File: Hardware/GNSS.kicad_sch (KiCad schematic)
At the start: 20 parts, among them J1 U.FL_SMD, Q3 BSS138, U13 74HC4052D, U2 mosaic-X5

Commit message: Work in progress...
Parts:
- added TP15, TP16, TP17, TP18: 1.0mm, SparkFun-Connector:TestPoint-1.0mm, symbol SparkFun-Connector:TestPoint_1.0mm
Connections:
- net ESP13/MTX1: now also TP15.1
- net ESP14/MRX1: now also TP16.1
- net ESP25/MRX4: now also TP17.1
- net ESP4/MTX4: now also TP18.1
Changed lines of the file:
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@@
   (junction (at 57.15 97.79) (diameter 0) (color 0 0 0 0)
   )
+  (junction (at 92.71 36.83) (diameter 0) (color 0 0 0 0)
+  )
   (junction (at 231.14 128.27) (diameter 0) (color 0 0 0 0)
   )
+  (junction (at 92.71 34.29) (diameter 0) (color 0 0 0 0)
+  )
   (junction (at 210.82 128.27) (diameter 0) (color 0 0 0 0)
   )
@@
   (junction (at 48.26 113.03) (diameter 0) (color 0 0 0 0)
   )
+  (junction (at 93.98 71.12) (diameter 0) (color 0 0 0 0)
+  )
   (junction (at 36.83 34.29) (diameter 0) (color 0 0 0 0)
   )
+  (junction (at 92.71 73.66) (diameter 0) (color 0 0 0 0)
+  )
   (wire (pts (xy 91.44 77.47) (xy 92.71 77.47))
     (stroke (width 0) (type default))
@@
     (stroke (width 0) (type default))
   )
+  (wire (pts (xy 95.25 66.04) (xy 92.71 66.04))
+    (stroke (width 0) (type default))
+  )
   (wire (pts (xy 22.86 86.36) (xy 22.86 85.09))
     (stroke (width 0) (type default))
@@
     (stroke (width 0) (type default))
   )
+  (wire (pts (xy 92.71 66.04) (xy 92.71 73.66))
+    (stroke (width 0) (type default))
+  )
   (wire (pts (xy 57.15 97.79) (xy 58.42 97.79))
     (stroke (width 0) (type default))
   )
+  (wire (pts (xy 92.71 31.75) (xy 92.71 34.29))
+    (stroke (width 0) (type default))
+  )
   (wire (pts (xy 55.88 97.79) (xy 57.15 97.79))
     (stroke (width 0) (type default))
   )
+  (wire (pts (xy 93.98 71.12) (xy 95.25 71.12))
+    (stroke (width 0) (type default))
+  )
   (wire (pts (xy 210.82 128.27) (xy 212.09 128.27))
     (stroke (width 0) (type default))
@@
     (stroke (width 0) (type default))
   )
-  (wire (pts (xy 91.44 71.12) (xy 92.71 71.12))
+  (wire (pts (xy 91.44 71.12) (xy 93.98 71.12))
     (stroke (width 0) (type default))
   )
@@
     (stroke (width 0) (type default))
   )
+  (wire (pts (xy 92.71 34.29) (xy 93.98 34.29))
+    (stroke (width 0) (type default))
+  )
   (wire (pts (xy 29.21 71.12) (xy 29.21 69.85))
     (stroke (width 0) (type default))
@@
     (stroke (width 0) (type default))
   )
+  (wire (pts (xy 92.71 36.83) (xy 92.71 39.37))
+    (stroke (width 0) (type default))
+  )
   (wire (pts (xy 223.52 128.27) (xy 231.14 128.27))
     (stroke (width 0) (type default))
@@
     (stroke (width 0) (type default))
   )
+  (wire (pts (xy 93.98 39.37) (xy 92.71 39.37))
+    (stroke (width 0) (type default))
+  )
   (wire (pts (xy 210.82 38.1) (xy 214.63 38.1))
     (stroke (width 0) (type default))
   )
+  (wire (pts (xy 93.98 68.58) (xy 93.98 71.12))
+    (stroke (width 0) (type default))
+  )
   (wire (pts (xy 34.29 34.29) (xy 36.83 34.29))
     (stroke (width 0) (type default))
@@
     (stroke (width 0) (type default))
   )
+  (wire (pts (xy 92.71 73.66) (xy 95.25 73.66))
+    (stroke (width 0) (type default))
+  )
   (wire (pts (xy 36.83 24.13) (xy 36.83 25.4))
     (stroke (width 0) (type default))
@@
     (stroke (width 0) (type default))
   )
+  (wire (pts (xy 95.25 68.58) (xy 93.98 68.58))
+    (stroke (width 0) (type default))
+  )
   (wire (pts (xy 87.63 167.64) (xy 86.36 167.64))
     (stroke (width 0) (type default))
@@
     (stroke (width 0) (type default))
   )
+  (wire (pts (xy 92.71 36.83) (xy 93.98 36.83))
+    (stroke (width 0) (type default))
+  )
   (wire (pts (xy 91.44 80.01) (xy 92.71 80.01))
     (stroke (width 0) (type default))
@@
   )
   (wire (pts (xy 57.15 44.45) (xy 57.15 48.26))
+    (stroke (width 0) (type default))
+  )
+  (wire (pts (xy 93.98 31.75) (xy 92.71 31.75))
     (stroke (width 0) (type default))
   )
@@
     )
   )
-  (global_label "ESP14{slash}MRX1" (shape input) (at 92.71 34.29 0) (fields_autoplaced)
-    (effects (font (size 1.27 1.27)) (justify left))
-    (property "Intersheetrefs" "${INTERSHEET_REFS}" (at 107.0041 34.29 0)
+  (global_label "ESP14{slash}MRX1" (shape input) (at 93.98 34.29 0) (fields_autoplaced)
+    (effects (font (size 1.27 1.27)) (justify left))
+    (property "Intersheetrefs" "${INTERSHEET_REFS}" (at 108.2741 34.29 0)
       (effects (font (size 1.27 1.27)) (justify left) hide)
     )
@@
     )
   )
-  (global_label "ESP25{slash}MRX4" (shape input) (at 92.71 71.12 0) (fields_autoplaced)
-    (effects (font (size 1.27 1.27)) (justify left))
-    (property "Intersheetrefs" "${INTERSHEET_REFS}" (at 108.2136 71.12 0)
+  (global_label "ESP25{slash}MRX4" (shape input) (at 95.25 71.12 0) (fields_autoplaced)
+    (effects (font (size 1.27 1.27)) (justify left))
+    (property "Intersheetrefs" "${INTERSHEET_REFS}" (at 110.7536 71.12 0)
       (effects (font (size 1.27 1.27)) (justify left) hide)
     )
@@
     )
   )
-  (global_label "ESP4{slash}MTX4" (shape input) (at 92.71 73.66 0) (fields_autoplaced)
-    (effects (font (size 1.27 1.27)) (justify left))
-    (property "Intersheetrefs" "${INTERSHEET_REFS}" (at 106.7017 73.66 0)
+  (global_label "ESP4{slash}MTX4" (shape input) (at 95.25 73.66 0) (fields_autoplaced)
+    (effects (font (size 1.27 1.27)) (justify left))
+    (property "Intersheetrefs" "${INTERSHEET_REFS}" (at 109.2417 73.66 0)
       (effects (font (size 1.27 1.27)) (justify left) hide)
     )
@@
     )
   )
-  (global_label "ESP13{slash}MTX1" (shape input) (at 92.71 36.83 0) (fields_autoplaced)
-    (effects (font (size 1.27 1.27)) (justify left))
-    (property "Intersheetrefs" "${INTERSHEET_REFS}" (at 106.7017 36.83 0)
+  (global_label "ESP13{slash}MTX1" (shape input) (at 93.98 36.83 0) (fields_autoplaced)
+    (effects (font (size 1.27 1.27)) (justify left))
+    (property "Intersheetrefs" "${INTERSHEET_REFS}" (at 107.9717 36.83 0)
       (effects (font (size 1.27 1.27)) (justify left) hide)
     )
@@
     )
   )
+  (symbol (lib_id "SparkFun-Connector:TestPoint_1.0mm") (at 93.98 31.75 270) (unit 1)
+    (in_bom yes) (on_board yes) (dnp no) (fields_autoplaced)
+    (property "Reference" "TP16" (at 99.06 31.75 90)
+      (effects (font (size 1.27 1.27)) (justify left))
+    )
+    (property "Value" "1.0mm" (at 90.17 31.75 0)
+      (effects (font (size 1.27 1.27)) hide)
+    )
+    (property "Footprint" "SparkFun-Connector:TestPoint-1.0mm" (at 87.63 31.75 0)
+      (effects (font (size 1.27 1.27)) hide)
+    )
+    (property "Datasheet" "~" (at 86.36 31.75 0)
+      (effects (font (size 1.27 1.27)) hide)
+    )
+    (pin "1")
+    (instances
+      (project "SparkFun_RTK_Facet_mosaic"
+        (path "/e3dd3ae4-244d-4cba-9cca-5d2abf83f29a/1004b21d-c362-4c5d-adad-4952c3ff3811"
+          (reference "TP16") (unit 1)
+        )
+      )
+    )
+  )
   (symbol (lib_id "SparkFun-Resistor:10k_0402") (at 53.34 115.57 0) (unit 1)
     (in_bom yes) (on_board yes) (dnp no)
@@
         (path "/e3dd3ae4-244d-4cba-9cca-5d2abf83f29a/1004b21d-c362-4c5d-adad-4952c3ff3811"
           (reference "#PWR010") (unit 1)
+        )
+      )
+    )
+  )
+  (symbol (lib_id "SparkFun-Connector:TestPoint_1.0mm") (at 93.98 39.37 270) (unit 1)
+    (in_bom yes) (on_board yes) (dnp no) (fields_autoplaced)
+    (property "Reference" "TP15" (at 97.282 41.91 90)
+      (effects (font (size 1.27 1.27)))
+    )
+    (property "Value" "1.0mm" (at 90.17 39.37 0)
+      (effects (font (size 1.27 1.27)) hide)
+    )
+    (property "Footprint" "SparkFun-Connector:TestPoint-1.0mm" (at 87.63 39.37 0)
+      (effects (font (size 1.27 1.27)) hide)
+    )
+    (property "Datasheet" "~" (at 86.36 39.37 0)
+      (effects (font (size 1.27 1.27)) hide)
+    )
+    (pin "1")
+    (instances
+      (project "SparkFun_RTK_Facet_mosaic"
+        (path "/e3dd3ae4-244d-4cba-9cca-5d2abf83f29a/1004b21d-c362-4c5d-adad-4952c3ff3811"
+          (reference "TP15") (unit 1)
         )
       )
@@
     )
   )
+  (symbol (lib_id "SparkFun-Connector:TestPoint_1.0mm") (at 95.25 68.58 270) (unit 1)
+    (in_bom yes) (on_board yes) (dnp no) (fields_autoplaced)
+    (property "Reference" "TP17" (at 100.33 68.58 90)
+      (effects (font (size 1.27 1.27)) (justify left))
+    )
+    (property "Value" "1.0mm" (at 91.44 68.58 0)
+      (effects (font (size 1.27 1.27)) hide)
+    )
+    (property "Footprint" "SparkFun-Connector:TestPoint-1.0mm" (at 88.9 68.58 0)
+      (effects (font (size 1.27 1.27)) hide)
+    )
+    (property "Datasheet" "~" (at 87.63 68.58 0)
+      (effects (font (size 1.27 1.27)) hide)
+    )
+    (pin "1")
+    (instances
+      (project "SparkFun_RTK_Facet_mosaic"
+        (path "/e3dd3ae4-244d-4cba-9cca-5d2abf83f29a/1004b21d-c362-4c5d-adad-4952c3ff3811"
+          (reference "TP17") (unit 1)
+        )
+      )
+    )
+  )
   (symbol (lib_id "SparkFun-Capacitor:22uF_0603_6.3V_20%") (at 29.21 66.04 0) (unit 1)
     (in_bom yes) (on_board yes) (dnp no) (fields_autoplaced)
@@
         )
       )
+    )
+  )
+  (symbol (lib_id "SparkFun-Connector:TestPoint_1.0mm") (at 95.25 66.04 270) (unit 1)
+    (in_bom yes) (on_board yes) (dnp no) (fields_autoplaced)
+    (property "Reference" "TP18" (at 100.33 66.04 90)
+      (effects (font (size 1.27 1.27)) (justify left))
+    )
+    (property "Value" "1.0mm" (at 91.44 66.04 0)
+      (effects (font (size 1.27 1.27)) hide)
+    )
+    (property "Footprint" "SparkFun-Connector:TestPoint-1.0mm" (at 88.9 66.04 0)
+      (effects (font (size 1.27 1.27)) hide)
+    )
+    (property "Datasheet" "~" (at 87.63 66.04 0)
+      (effects (font (size 1.27 1.27)) hide)
+    )
+    (pin "1")
+    (instances
+      (project "SparkFun_RTK_Facet_mosaic"
+        (path "/e3dd3ae4-244d-4cba-9cca-5d2abf83f29a/1004b21d-c362-4c5d-adad-4952c3ff3811"
+          (reference "TP18") (unit 1)
+        )
+      )

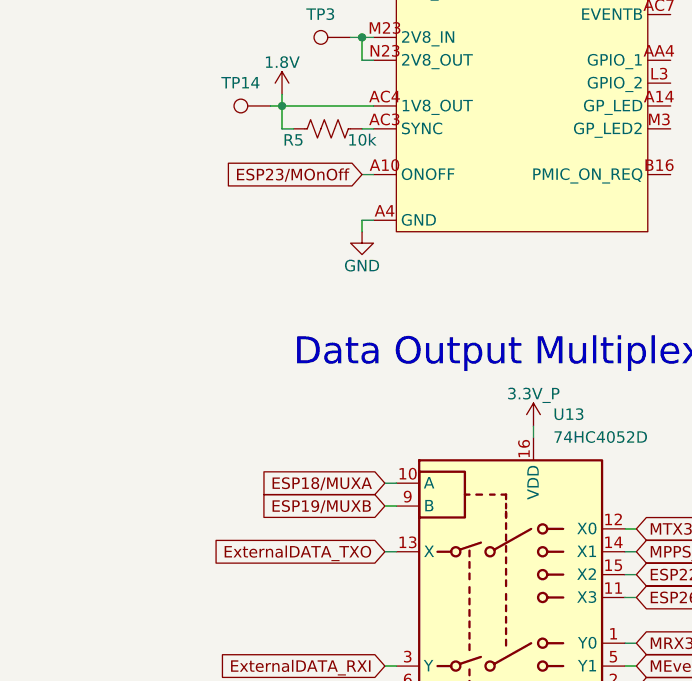
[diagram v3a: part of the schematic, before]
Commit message: Do over with RSP32 Pico Mini - routed
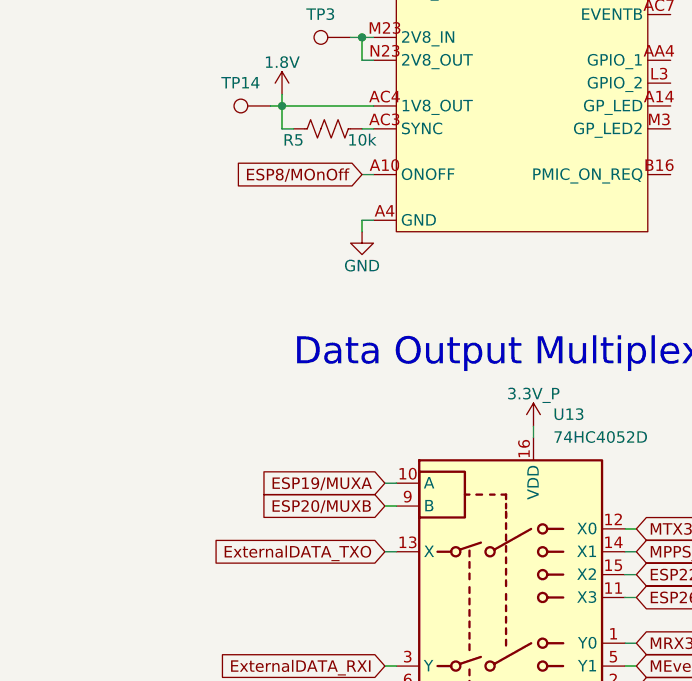
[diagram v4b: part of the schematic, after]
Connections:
- net ESP18/MUXA renamed ESP19/MUXA
- net ESP19/MUXB renamed ESP20/MUXB
- net ESP23/MOnOff renamed ESP8/MOnOff
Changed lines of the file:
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@@
     )
   )
-  (global_label "ESP19{slash}MUXB" (shape input) (at 59.69 157.48 180) (fields_autoplaced)
+  (global_label "ESP20{slash}MUXB" (shape input) (at 59.69 157.48 180) (fields_autoplaced)
     (effects (font (size 1.27 1.27)) (justify right))
     (property "Intersheetrefs" "${INTERSHEET_REFS}" (at 44.0654 157.48 0)
@@
     )
   )
-  (global_label "ESP23{slash}MOnOff" (shape input) (at 57.15 120.65 180) (fields_autoplaced)
+  (global_label "ESP8{slash}MOnOff" (shape input) (at 57.15 120.65 180) (fields_autoplaced)
     (effects (font (size 1.27 1.27)) (justify right))
     (property "Intersheetrefs" "${INTERSHEET_REFS}" (at 40.074 120.65 0)
@@
     )
   )
-  (global_label "ESP18{slash}MUXA" (shape input) (at 59.69 154.94 180) (fields_autoplaced)
+  (global_label "ESP19{slash}MUXA" (shape input) (at 59.69 154.94 180) (fields_autoplaced)
     (effects (font (size 1.27 1.27)) (justify right))
     (property "Intersheetrefs" "${INTERSHEET_REFS}" (at 44.2468 154.94 0)

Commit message: Switching back to the WROVER - routed
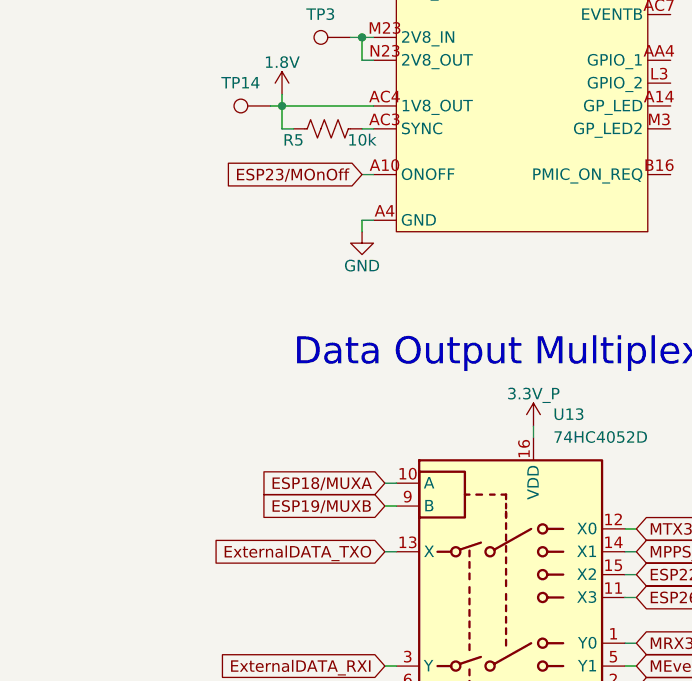
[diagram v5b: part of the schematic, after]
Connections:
- net ESP19/MUXA renamed ESP18/MUXA
- net ESP20/MUXB renamed ESP19/MUXB
- net ESP8/MOnOff renamed ESP23/MOnOff
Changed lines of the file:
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@@
     )
   )
-  (global_label "ESP20{slash}MUXB" (shape input) (at 59.69 157.48 180) (fields_autoplaced)
+  (global_label "ESP19{slash}MUXB" (shape input) (at 59.69 157.48 180) (fields_autoplaced)
     (effects (font (size 1.27 1.27)) (justify right))
     (property "Intersheetrefs" "${INTERSHEET_REFS}" (at 44.0654 157.48 0)
@@
     )
   )
-  (global_label "ESP8{slash}MOnOff" (shape input) (at 57.15 120.65 180) (fields_autoplaced)
+  (global_label "ESP23{slash}MOnOff" (shape input) (at 57.15 120.65 180) (fields_autoplaced)
     (effects (font (size 1.27 1.27)) (justify right))
     (property "Intersheetrefs" "${INTERSHEET_REFS}" (at 40.074 120.65 0)
@@
     )
   )
-  (global_label "ESP19{slash}MUXA" (shape input) (at 59.69 154.94 180) (fields_autoplaced)
+  (global_label "ESP18{slash}MUXA" (shape input) (at 59.69 154.94 180) (fields_autoplaced)
     (effects (font (size 1.27 1.27)) (justify right))
     (property "Intersheetrefs" "${INTERSHEET_REFS}" (at 44.2468 154.94 0)

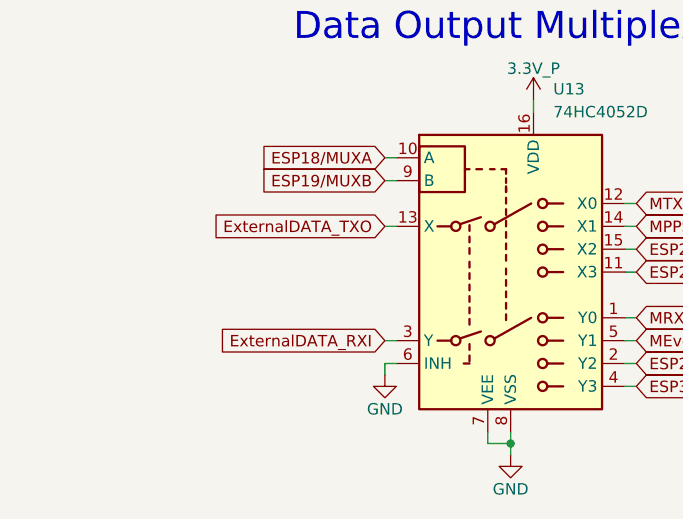
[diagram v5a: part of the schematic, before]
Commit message: Add extra Test Points
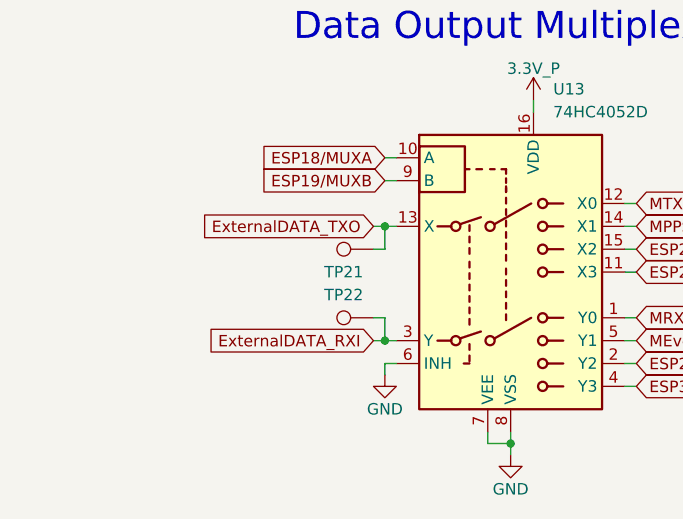
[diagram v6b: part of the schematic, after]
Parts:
- added TP21, TP22: PTH, SparkFun-Connector:1X01, symbol SparkFun-Connector:TestPoint_PTH
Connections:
- net ExternalDATA_RXI: now also TP22.1
- net ExternalDATA_TXO: now also TP21.1

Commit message: v1.1 routed
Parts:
- removed J1: U.FL_SMD, SparkFun-Connector:U.FL, symbol SparkFun-RF:U.FL_SMD
- added J1: U.FL, SparkFun-Connector:U.FL, symbol SparkFun-RF:U.FL
- TP21, TP22, TP6: footprint SparkFun-Connector:1X01 -> SparkFun-Connector:1x01
- U13: footprint SparkFun-Semiconductor-Standard:SO16 -> SparkFun-Semiconductor-Standard:SO-16
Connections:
- net GND: now also J1.2 (Ext)
- net MOSAIC_RF_IN: now also J1.1 (In)
- net ESP18/MUXA renamed ESP2/MUXA
- net ESP19/MUXB renamed ESP12/MUXB
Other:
- moved on the sheet: C26, C27, C28, C29, C3, D1, L1, Q3, R11, R12, R13, R16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

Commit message: V1.1 Panelized
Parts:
- added R41: 169k, SparkFun-Resistor:R_0603_1608Metric, symbol SparkFun-Resistor:169k_0603
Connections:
- net at U2.AC7 (EVENTB): now also R41.2
- new net ESP18/MEventB: R41.1
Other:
- note added: "1.8V Inputs protected by 169k/200k divider"
- note removed: "1.8V Input protected by 169k/200k divider"
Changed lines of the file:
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@@
 	(wire
 		(pts
+			(xy 106.68 104.14) (xy 107.95 104.14)
+		)
+		(stroke
+			(width 0)
+			(type default)
+		)
+	)
+	(wire
+		(pts
 			(xy 210.82 137.16) (xy 212.09 137.16)
 		)
@@
 	(wire
 		(pts
+			(xy 97.79 104.14) (xy 99.06 104.14)
+		)
+		(stroke
+			(width 0)
+			(type default)
+		)
+	)
+	(wire
+		(pts
 			(xy 63.5 106.68) (xy 63.5 109.22)
 		)
@@
 	(text "PPS Level-Shifting\n"
 		(exclude_from_sim no)
-		(at 196.85 118.11 0)
+		(at 201.93 117.094 0)
 		(effects
 			(font
@@
 		)
 	)
-	(text "1.8V Input protected by 169k/200k divider"
+	(text "1.8V Inputs protected by 169k/200k divider"
 		(exclude_from_sim no)
-		(at 120.65 102.87 0)
+		(at 125.984 103.632 0)
 		(effects
 			(font
@@
 		)
 	)
+	(global_label "ESP18{slash}MEventB"
+		(shape input)
+		(at 107.95 104.14 0)
+		(fields_autoplaced yes)
+		(effects
+			(font
+				(size 1.27 1.27)
+			)
+			(justify left)
+		)
+		(property "Intersheetrefs" "${INTERSHEET_REFS}"
+			(at 124.6631 104.14 0)
+			(effects
+				(font
+					(size 1.27 1.27)
+				)
+				(justify left)
+				(hide yes)
+			)
+		)
+	)
 	(global_label "ExternalDATA_TXO"
 		(shape input)
@@
 		(dnp no)
 		(property "Reference" "R16"
-			(at 102.87 99.06 0)
+			(at 100.33 99.314 0)
 			(effects
 				(font
@@
 		)
 		(property "Value" "169k"
-			(at 102.87 104.14 0)
+			(at 105.41 99.314 0)
 			(effects
 				(font
@@
 					(unit 1)
 				)
+			)
+		)
+	)
+	(symbol
+		(lib_id "SparkFun-Resistor:169k_0603")
+		(at 102.87 104.14 0)
+		(mirror x)
+		(unit 1)
+		(exclude_from_sim no)
+		(in_bom yes)
+		(on_board yes)
+		(dnp no)
+		(property "Reference" "R41"
+			(at 100.33 106.426 0)
+			(effects
+				(font
+					(size 1.27 1.27)
+				)
+			)
+		)
+		(property "Value" "169k"
+			(at 105.41 106.426 0)
+			(effects
+				(font
+					(size 1.27 1.27)
+				)
+			)
+		)
+		(property "Footprint" "SparkFun-Resistor:R_0603_1608Metric"
+			(at 102.87 99.822 0)
+			(effects
+				(font
+					(size 1.27 1.27)
+				)
+				(hide yes)
+			)
+		)
+		(property "Datasheet" "https://www.vishay.com/docs/20035/dcrcwe3.pdf"
+			(at 102.87 95.25 0)
+			(effects
+				(font
+					(size 1.27 1.27)
+				)
+				(hide yes)
+			)
+		)
+		(property "Description" "Resistor"
+			(at 102.87 104.14 0)
+			(effects
+				(font
+					(size 1.27 1.27)
+				)
+				(hide yes)
+			)
+		)
+		(property "PROD_ID" "RES-14394"
+			(at 102.87 97.79 0)
+			(effects
+				(font
+					(size 1.27 1.27)
+				)
+				(hide yes)
+			)
+		)
+		(pin "1"
+		)
+		(pin "2"
+		)
+		(instances
+			(project "SparkFun_RTK_Facet_mosaic"
+				(path "/e3dd3ae4-244d-4cba-9cca-5d2abf83f29a/1004b21d-c362-4c5d-adad-4952c3ff3811"
+					(reference "R41")
+					(unit 1)
+				)
